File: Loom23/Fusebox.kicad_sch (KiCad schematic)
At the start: 8 parts

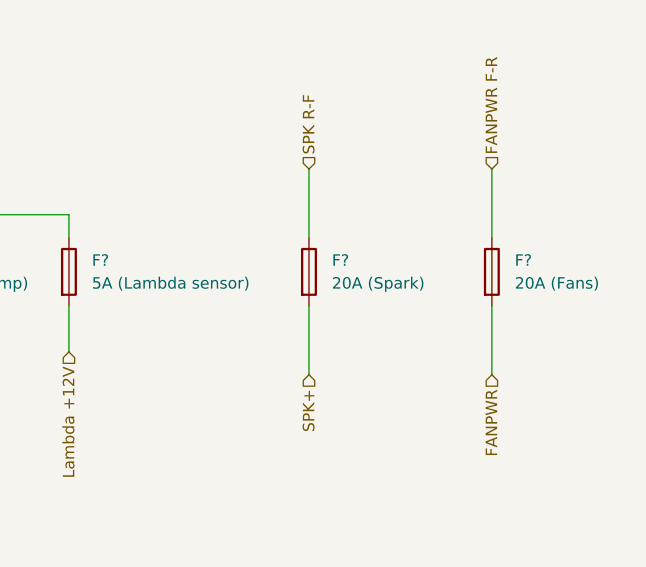
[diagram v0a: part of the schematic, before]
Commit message: Added connector pinouts
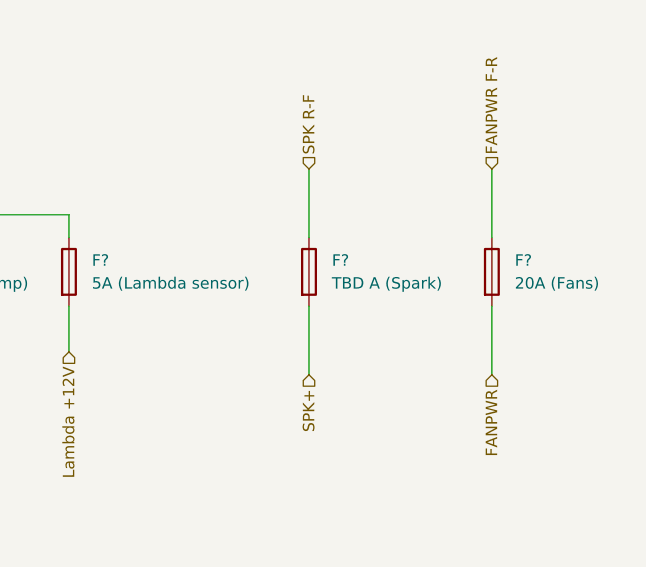
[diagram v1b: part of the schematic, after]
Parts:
- F?: value 20A (Spark) -> TBD A (Spark)
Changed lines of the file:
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@@
       (effects (font (size 1.27 1.27)) (justify left))
     )
-    (property "Value" "20A (Spark)" (id 1) (at 215.9 78.7399 0)
+    (property "Value" "TBD A (Spark)" (id 1) (at 215.9 78.7399 0)
       (effects (font (size 1.27 1.27)) (justify left))
     )
